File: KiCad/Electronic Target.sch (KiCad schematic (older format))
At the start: 47 parts, among them J1 Conn_02x06_Odd_Even, J2 Conn_02x04_Odd_Even, U1 LM339, U2 74HC74, U3 74HC74, U4 74HC00, U5 74LV8154, U6 74LV8154, U7 NMA0505SC, X1 8M0

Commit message: Changed to I2C Temperature Sensor
The older RTD temperature sensor was replaced by an I2C one located on the main board.

This also brough in changes to the sensor module and additional data on the JSON shot info
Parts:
- added U8: LM75AIMX_NOPB, Package_SO:SOIC-8_3.9x4.9mm_P1.27mm, symbol 2020-05-12_18-19-55:LM75AIMX_NOPB
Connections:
- net GND: now also U8.4 (GND)
- net VCC: now also U8.5 (A2), U8.6 (A1), U8.7 (A0), U8.8 (VS+)
- net at XA1.D20 (D20_SDA): now also U8.1 (SDA)
- net at XA1.D21 (D21_SCL): now also U8.2 (SCL)
- net SCL: no longer names the net of XA1.SCL
- net SCL: no longer J1.12 (Pin_12)
- net SDA: no longer names the net of XA1.SDA
- net SDA: no longer J1.10 (Pin_10)
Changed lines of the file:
@@
 	700  1600 700  1700
 Connection ~ 700  1700
+$Comp
+L 2020-05-12_18-19-55:LM75AIMX_NOPB U8
+U 1 1 5ED0FC30
+P 13400 1900
+F 0 "U8" H 14500 2287 60  0000 C CNN
+F 1 "LM75AIMX_NOPB" H 14500 2181 60  0000 C CNN
+F 2 "Package_SO:SOIC-8_3.9x4.9mm_P1.27mm" H 14500 2140 60  0001 C CNN
+F 3 "" H 13400 1900 60  0000 C CNN
+	1    13400 1900
+	1    0    0    -1
+$EndComp
+Connection ~ 15600 1900
 Wire Wire Line
-	15700 4500 15350 4500
+	15600 1900 15600 2000
+Connection ~ 15600 2000
 Wire Wire Line
-	15700 4600 15350 4600
-Text Label 15450 4500 0    50   ~ 0
-SDA
-Text Label 15450 4600 0    50   ~ 0
-SCL
+	15600 2000 15600 2100
+Connection ~ 15600 2100
 Wire Wire Line
-	1200 1700 1700 1700
+	15600 2100 15600 2200
+$Comp
+L power:VCC #PWR0104
+U 1 1 5ED30C38
+P 15600 1500
+F 0 "#PWR0104" H 15600 1350 50  0001 C CNN
+F 1 "VCC" H 15615 1673 50  0000 C CNN
+F 2 "" H 15600 1500 50  0001 C CNN
+F 3 "" H 15600 1500 50  0001 C CNN
+	1    15600 1500
+	1    0    0    -1
+$EndComp
 Wire Wire Line
-	1200 1600 1700 1600
-Text Label 1350 1600 0    50   ~ 0
-SDA
-Text Label 1350 1700 0    50   ~ 0
-SCL
+	15600 1500 15600 1900
+$Comp
+L power:GND #PWR0105
+U 1 1 5ED711A0
+P 13400 2450
+F 0 "#PWR0105" H 13400 2200 50  0001 C CNN
+F 1 "GND" H 13405 2277 50  0000 C CNN
+F 2 "" H 13400 2450 50  0001 C CNN
+F 3 "" H 13400 2450 50  0001 C CNN
+	1    13400 2450
+	1    0    0    -1
+$EndComp
+Wire Wire Line
+	13400 2200 13400 2450
+Wire Wire Line
+	13400 2000 13300 2000
+Wire Wire Line
+	13300 2000 13300 2850
+Wire Wire Line
+	13300 2850 15750 2850
+Wire Wire Line
+	13200 1900 13200 2950
+Wire Wire Line
+	13200 2950 15650 2950
+Wire Wire Line
+	13200 1900 13400 1900
+Wire Wire Line
+	15650 2950 15650 4300
+Wire Wire Line
+	15650 4300 15350 4300
+Wire Wire Line
+	15350 4400 15750 4400
+Wire Wire Line
+	15750 4400 15750 2850
 $EndSCHEMATC

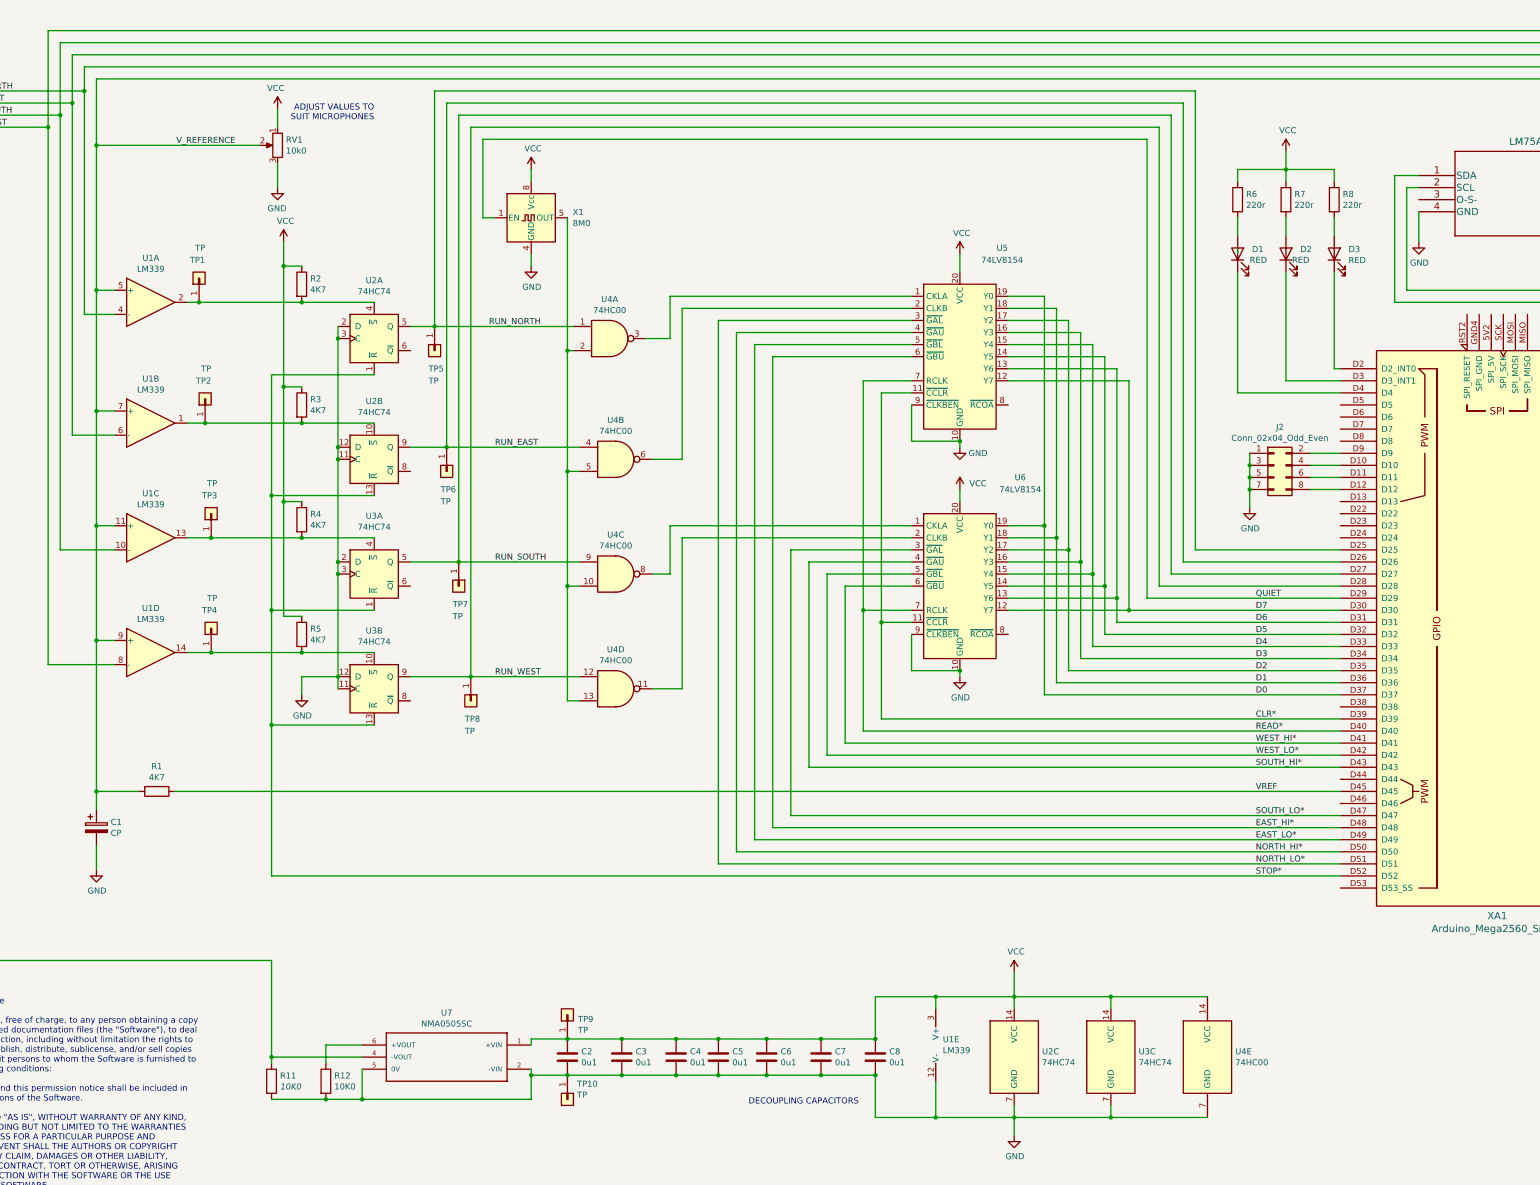
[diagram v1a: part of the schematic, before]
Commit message: Adding DigiKey part numbers
Adding in DK part numbers for manufacturing
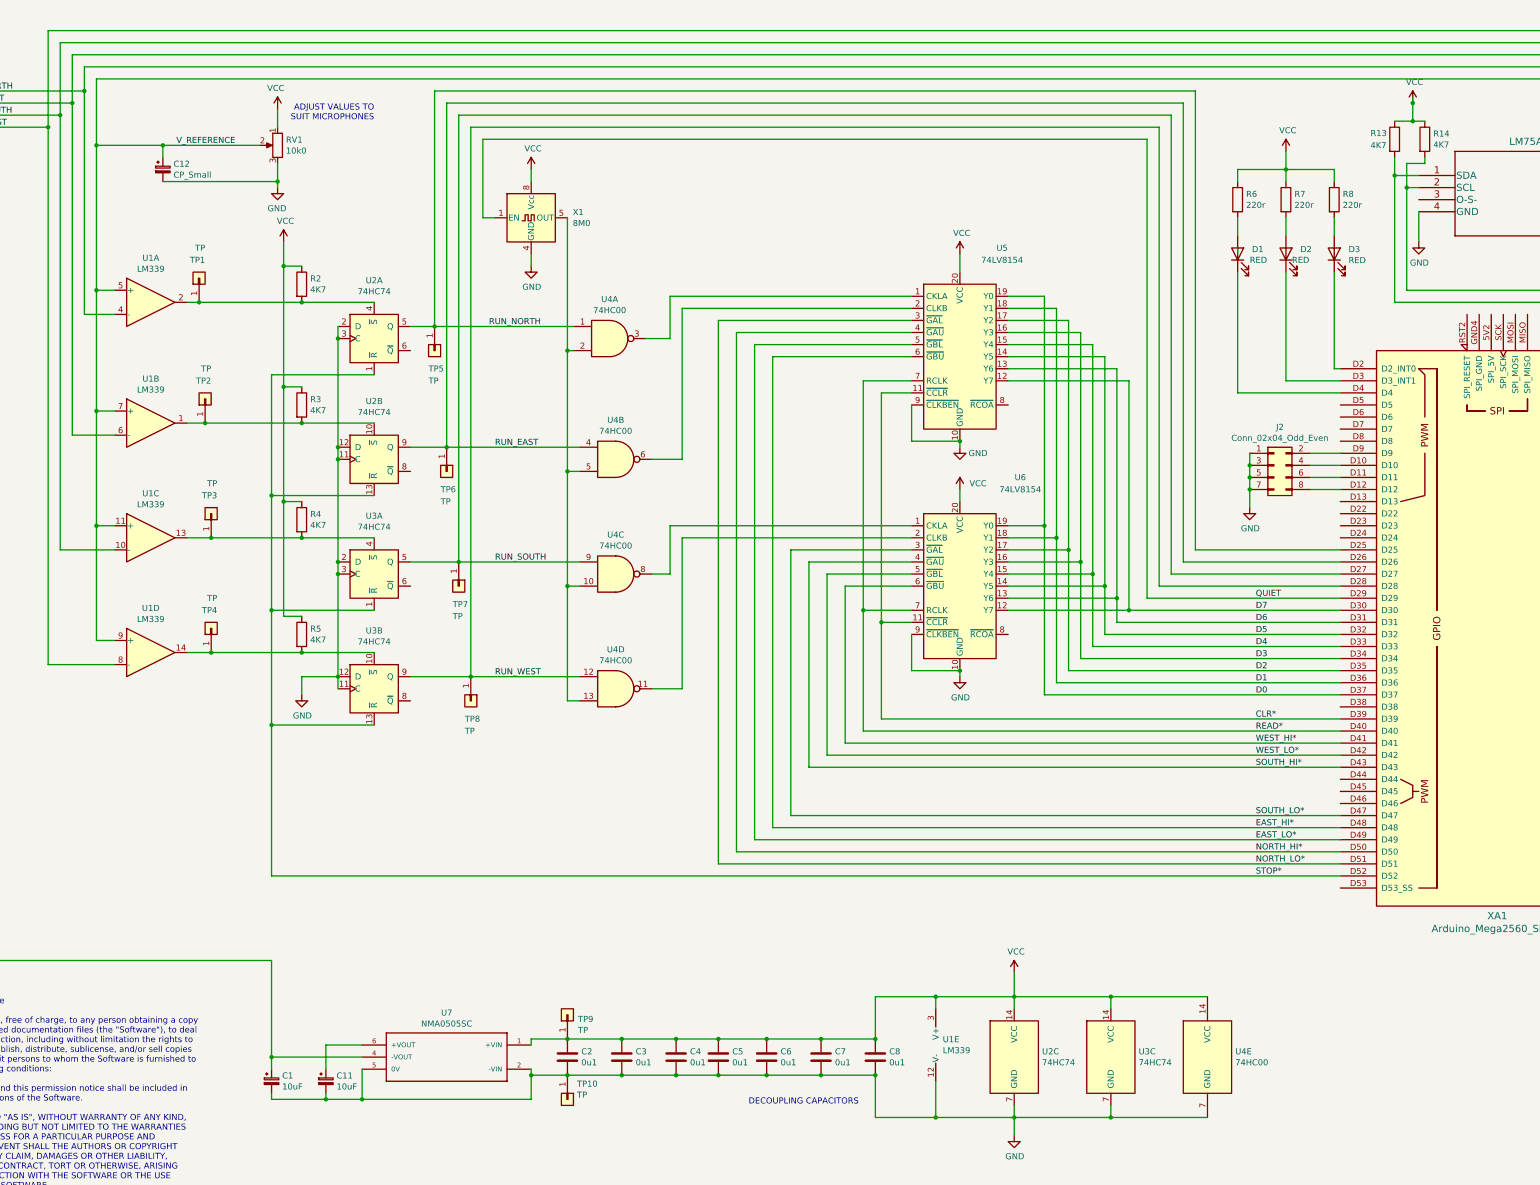
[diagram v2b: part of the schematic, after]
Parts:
- removed C1: CP, Resistor_SMD:R_1812_4532Metric, symbol Device:CP
- removed R1: 4K7, Resistor_SMD:R_0805_2012Metric, symbol Device:R
- removed R11, R12: 10K0, Resistor_SMD:R_0805_2012Metric, symbol Device:R
- added C1, C11: 10uF, Resistor_SMD:R_1206_3216Metric, symbol Device:CP_Small
- added C12: CP_Small, Resistor_SMD:R_1206_3216Metric, symbol Device:CP_Small
- added R13, R14: 4K7, Resistor_SMD:R_0805_2012Metric, symbol Device:R
- C10: Digikey (none) -> 478-10742-1-ND
- R2, R3, R4, R5: DigiKey (none) -> 311-4.70KCRCT-ND
- R6, R7, R8: DigiKey (none) -> A126351CT-ND
- RV1: DigiKey (none) -> 987-1014-1-ND
- U1: DigiKey (none) -> 296-1013-1-ND
- U1: DigiKey (none) -> 293-1013-1-ND
- U2, U3: DigiKey (none) -> 296-1204-1-ND
- U4: DigiKey (none) -> 296-1187-1-ND
- U5, U6: DigiKey (none) -> 296-47353-1-ND
- X1: DigiKey (none) -> 110-MXO45HST-3C-8M000000-ND
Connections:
- net GND: now also C1.2, C11.2, C12.2
- net VCC: now also R13.1, R14.1
- net V_FB: now also C12.1
- net at U8.1 (SDA), XA1.D20 (D20_SDA): now also R13.2
- net at U8.2 (SCL), XA1.D21 (D21_SCL): now also R14.2
- net at C10.1, J1.11 (Pin_11), J1.9 (Pin_9)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: now also C1.1
- net at U7.6 (+VOUT): now also C11.1
- net VREF: no longer names the net of XA1.D45
